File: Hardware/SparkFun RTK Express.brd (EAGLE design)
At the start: 68.2 x 110.1 mm, 198 parts, among them J13 Internal, J16 microSD, J17 Qwiic Right Angle, J19 FPC_12_0.5MM_BACKFLIP, J3 USB Female Type C Connector, J4 External, J5 USB Female Type C Connector, Q1 SIL2308-TP, Q10 20V/0.2A/8MHz/1.2Ω/1Vth, Q2 MBT3904DW1T1, Q3 20V/0.2A/8MHz/1.2Ω/1Vth, Q4 20V/0.2A/8MHz/1.2Ω/1Vth, Q7 20V/0.2A/8MHz/1.2Ω/1Vth, Q9 20V/0.2A/8MHz/1.2Ω/1Vth, U1 74HC4052D, U10 MCP73833, U13 9DoF IMU, U14 1.8V/100mA, U2 AP2112K-3.3, U3 U-BLOX_ZED-F9P, U4 ADP160, U5 ESP-WROOM-32NARROW, U6 CH340C, U7 MAX17048

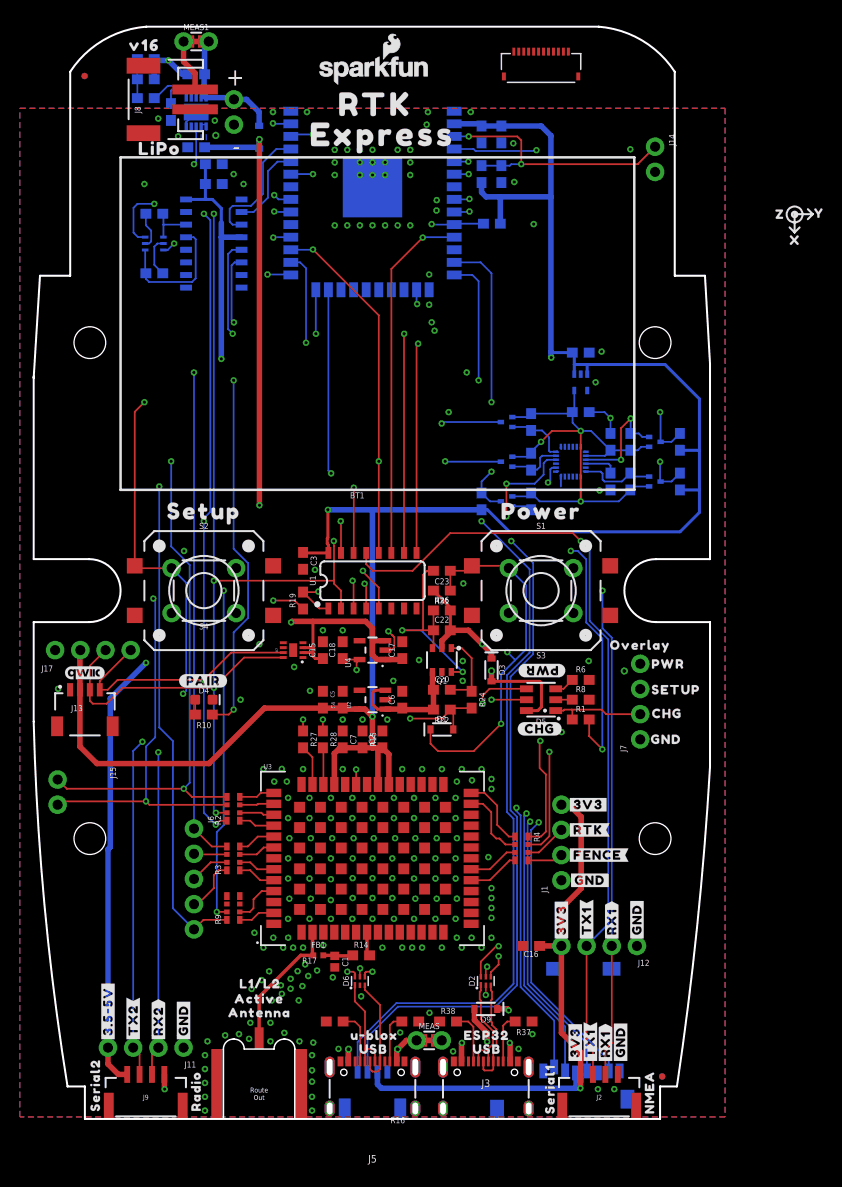
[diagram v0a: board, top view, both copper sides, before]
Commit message: Ready v11. Redo GND layers for panelizer.
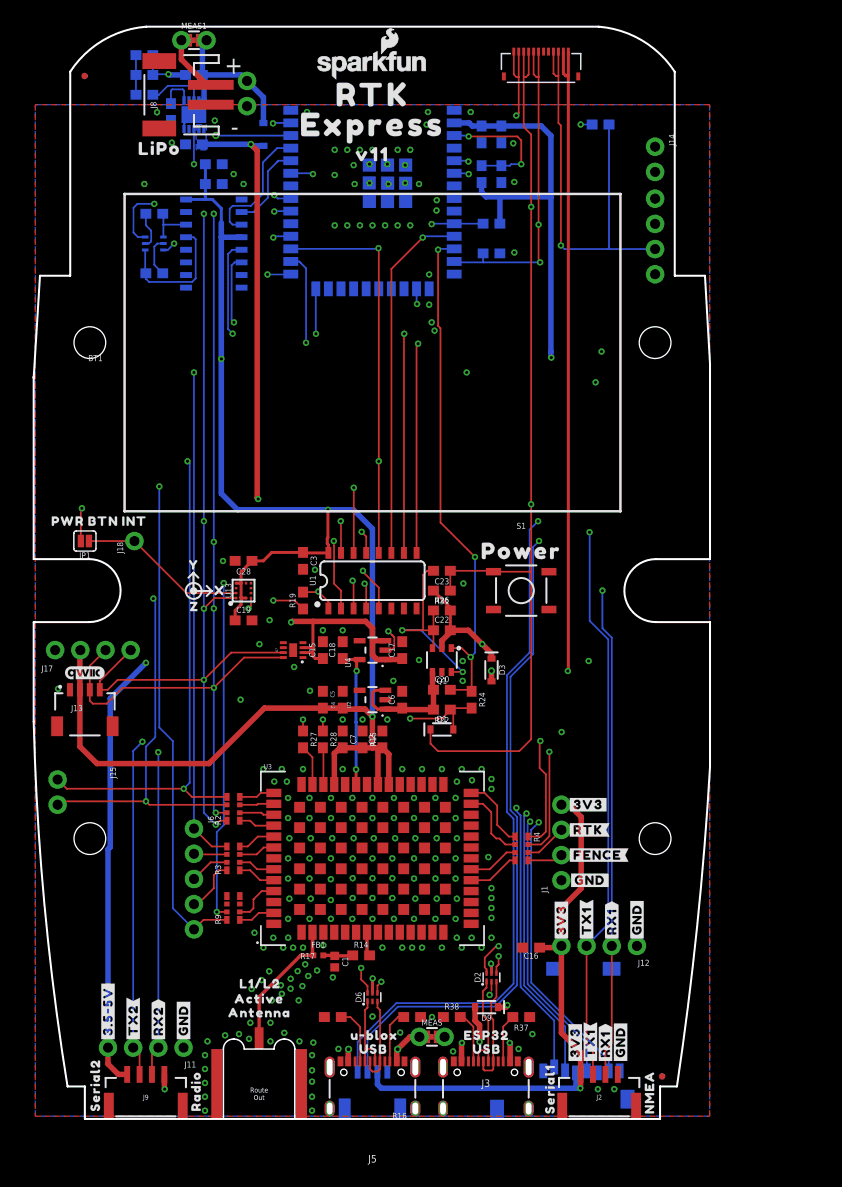
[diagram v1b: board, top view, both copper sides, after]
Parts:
- removed C51, C52: 0.1uF, SparkFun-Capacitors:0603
- removed C53, C54: 1.0uF, SparkFun-Capacitors:0603
- removed D4: BLUE, SparkFun-LED:LED-0603
- removed D5: RGB, SparkFun-LED:PLCC-6-LED
- removed Q10, Q3, Q4, Q7, Q9: 20V/0.2A/8MHz/1.2Ω/1Vth, SparkFun-DiscreteSemi:SOT-416FL
- removed R10: 330, SparkFun-Resistors:0603
- removed R40, R41, R44, R45, R46, R47, R48: 2.2k, SparkFun-Resistors:0603
- removed R49: (no value), SparkFun-Resistors:0603
- removed R6, R8: 1k, SparkFun-Resistors:0603
- removed S2: Setup, SparkFun-Switches:TACTILE_SWITCH_PTH_6.0MM
- removed S3: Power, SparkFun-Switches:TACTILE_SWITCH_SMD_12MM
- removed S4: Setup, SparkFun-Switches:TACTILE_SWITCH_SMD_12MM
- removed U$12, U$22: (no value), output:X1
- removed U$13, U$76: (no value), SparkFun GPS RTK Surveyor:LIGHT_PIPE_3MM
- removed U$15, U$21: (no value), output:Y2
- removed U$20: (no value), output:#PAIR#0
- removed U$25: (no value), output:#PWR#2
- removed U$44: (no value), output:OVERLAY0
- removed U$52, U$54: (no value), output:Z0
- removed U$95: (no value), output:AG0
- removed U$96: (no value), output:M0
- removed U14: 1.8V/100mA, SparkFun-IC-Power:SC70
- added C19: 10uF, SparkFun-Capacitors:0603
- added C21, C28: 0.1uF, SparkFun-Capacitors:0603
- added J18: (no value), SparkFun-Connectors:1X01_NO_SILK
- added JP1: (no value), SparkFun-Jumpers:SMT-JUMPER_2_NO_SILK
- BT1: value LIPO-OUTLINE1100 -> LIPO-OUTLINE1000
- R1: value 4.7k -> 470
- S1: device SparkFun-Switches:TACTILE_SWITCH_PTH_6.0MM -> SparkFun-Switches:TACTILE_SWITCH_SMD_5.2MM
- U$4: device output:V160 -> output:INT0
- U$8: device output:#CHG#0 -> output:V110
- U$9: device output:SETUP0 -> output:PWR_BTN1
- U13: value 9DoF IMU -> LIS2DH12; device SparkFun-Sensors:QFN24-3X3-ICM-20948 -> SparkFun-Sensors:LGA-12-LISDH12
- U5: value ESP-WROOM-32NARROW -> ESP-WROOM-3232D-NARROW; device SparkFun-RF:ESP-WROOM-32-NARROW -> SparkFun-RF:ESP-WROOM-32D-NARROW
- moved U$55 72.3 mm to (17.0, 55.6)
- moved U$56 71.1 mm to (16.9, 51.4)
- moved U$24 67.8 mm to (19.6, 53.0), turned to 0 degrees
- moved U$8 60.3 mm to (35.0, 97.0)
- moved R1 60.0 mm to (58.0, 100.0), flipped to the bottom
- moved U$4 48.0 mm to (11.0, 60.0)
- moved U$42 47.2 mm to (59.9, 89.9), flipped to the bottom
- moved U$41 47.1 mm to (60.7, 92.5), flipped to the bottom
- moved U$33 47.1 mm to (60.8, 87.5), flipped to the bottom
- moved U$34 47.0 mm to (60.9, 84.9), flipped to the bottom
- moved J7 46.9 mm to (63.5, 84.9), flipped to the bottom
- moved U$53 44.0 mm to (35.0, 50.0)
- moved U13 35.5 mm to (22.0, 53.0), flipped to the top, turned to 90 degrees
- moved BT1 29.8 mm to (35.0, 77.0)
- moved U$9 12.0 mm to (6.00, 60.0)
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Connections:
- net RTC_BACKUP renamed V_BKCP
- removed net ESP_12/LED_BLUETOOTH: R10.1, U5.14
- removed net ESP_15/ICM_!CS!: Q9.3, R47.1, U5.23
- removed net ESP_32/PWR_LVL_RED: D5.AR, U5.8
- removed net ESP_33/PWR_LVL_GRN: D5.AG, U5.9
- removed net ESP_I36/ICM_INT: Q7.3, R45.1, U5.4
- removed net ICM-20948-LV_!CS!: Q9.2, R46.1, U13.22
- removed net ICM-20948-LV_#_1.8V: C52.1, C53.1, Q10.1, Q3.1, Q4.1, Q7.1, Q9.1, R40.2, R41.2, R44.2, R46.2, R48.2, U13.13, U13.8, U14.5
- removed net ICM-20948-LV_INT: Q7.2, R44.1, U13.12
- removed net ICM-20948-LV_SCK: Q3.2, R40.1, U13.23
- removed net ICM-20948-LV_SDI: Q4.2, R41.1, U13.24
- removed net ICM-20948-LV_SDO: Q10.2, R48.1, U13.9
- removed net N$10: D5.CG, R6.1
- removed net N$14: D5.CR, R8.1
- removed net N$3: D4.A, R10.2
- removed net N$30: C51.1, U13.10
- new net ESP_12: U5.14
- new net ESP_15: U5.23
- new net ESP_32: U5.8
- new net ESP_33: U5.9
- new net ESP_4/ACCEL_INT: J18.1, JP1.1, U13.12
- new net ESP_I36: U5.4
- net 3.3V: now also C19.1, C28.1, U13.10, U13.2, U13.3, U13.9; no longer C54.1, R45.2, R47.2, R49.2, U14.1, U14.3
- net CHG_LED: no longer J19.10, J19.9
- net CHG_LED_RES: now also J19.10, J19.9; no longer D5.CB
- net ESP_14/SETUP_BUTTON: now also C21.1; no longer S2.1, S4.1
- net ESP_18/SCK: no longer Q3.3
- net ESP_19/CIPO: no longer Q10.3, R49.1
- net ESP_21/SDA: now also U13.4
- net ESP_22/SCL: now also U13.1
- net ESP_23/COPI: no longer Q4.3
- net GND: now also C19.2, C21.2, C28.2, U13.5, U13.6, U13.7, U13.8, U5.GND1, U5.GNDT1, U5.GNDT2, U5.GNDT3, U5.GNDT4, U5.GNDT5, U5.GNDT6, U5.GNDT7, U5.GNDT8; no longer C51.2, C52.2, C53.2, C54.2, D4.C, R6.2, R8.2, S2.3, S3.3, S4.3, U13.18, U13.20, U14.2, U5.GND
- net POWER_BTN: now also JP1.2; no longer S3.1
- net V_USB: no longer D5.AB
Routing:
- net POWER_BTN: track 50.7 -> 157.1 mm, vias 2 -> 3
- net ESP_14/SETUP_BUTTON: track 133.0 -> 45.6 mm, vias 3 -> 2
- net ESP_12/LED_BLUETOOTH: track 74.2 -> 0.00 mm, vias 3 -> 0
- net CHG_LED: track 107.6 -> 46.5 mm, vias 4 -> 2
- net ESP_33/PWR_LVL_GRN: track 60.9 -> 0.00 mm, vias 2 -> 0
- net ESP_32/PWR_LVL_RED: track 60.8 -> 0.00 mm, vias 2 -> 0
- net ESP_I36/ICM_INT: track 55.0 -> 0.00 mm, vias 3 -> 0
- net ICM-20948-LV_#_1.8V: track 53.9 -> 0.00 mm, vias 3 -> 0
- net V_USB: track 95.3 -> 140.7 mm
- net ESP_27/FAST_OFF: track 8.03 -> 52.5 mm, vias 0 -> 3
- net ESP_15/ICM_!CS!: track 39.7 -> 0.00 mm, vias 2 -> 0
- net CHG_LED_RES: track 9.78 -> 44.7 mm, vias 0 -> 1
- net 3.3V: track 349.6 -> 317.2 mm
- net ESP_19/CIPO: track 143.0 -> 115.7 mm, vias 5 -> 3
- net ESP_4/ACCEL_INT: track 0.00 -> 17.0 mm
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
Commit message: Update FP and PROD ID on ESP32 module
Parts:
- U4: value ADP160 -> STLQ015-3.3V
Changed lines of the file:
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@@
 <setting verticaltext="up"/>
 </settings>
-<grid distance="1" unitdist="mm" unit="mm" style="lines" multiple="1" display="yes" altdistance="0.1" altunitdist="mm" altunit="mm"/>
+<grid distance="0.05" unitdist="inch" unit="inch" style="lines" multiple="1" display="yes" altdistance="0.005" altunitdist="inch" altunit="inch"/>
 <layers>
 <layer number="1" name="Top/Horz" color="4" fill="1" visible="yes" active="yes"/>
-<layer number="2" name="GND/Horz" color="1" fill="3" visible="yes" active="yes"/>
-<layer number="15" name="Vert" color="4" fill="6" visible="yes" active="yes"/>
+<layer number="2" name="GND/Horz" color="1" fill="3" visible="no" active="yes"/>
+<layer number="15" name="Vert" color="4" fill="6" visible="no" active="yes"/>
 <layer number="16" name="Bottom/Vert" color="1" fill="1" visible="yes" active="yes"/>
 <layer number="17" name="Pads" color="2" fill="1" visible="yes" active="yes"/>
@@
 <attribute name="VALUE" value="470" x="58" y="99.238" size="0.6096" layer="28" font="vector" ratio="20" rot="MR0" align="top-center"/>
 </element>
-<element name="U4" library="SparkFun-IC-Power" package="SOT23-5" value="ADP160" x="35" y="47" smashed="yes" rot="R90">
+<element name="U4" library="SparkFun-IC-Power" package="SOT23-5" value="STLQ015-3.3V" x="35" y="47" smashed="yes" rot="R90">
 <attribute name="NAME" x="32.841" y="45.222" size="0.6096" layer="25" ratio="20" rot="R90"/>
-<attribute name="PROD_ID" value="VREG-11306" x="35" y="47" size="1.778" layer="27" font="vector" ratio="15" rot="R90" display="off"/>
-<attribute name="VALUE" value="ADP160" x="37.794" y="45.222" size="0.6096" layer="27" ratio="20" rot="R90"/>
+<attribute name="PROD_ID" value="IC-15779" x="35" y="47" size="1.778" layer="27" font="vector" ratio="15" rot="R90" display="off"/>
 </element>
 <element name="C17" library="SparkFun-Capacitors" package="0603" value="1.0uF" x="38" y="47" smashed="yes" rot="R90">
@@
 <element name="U5" library="SparkFun-RF" package="ESP-WROOM-32D-NARROW" value="ESP-WROOM-3232D-NARROW" x="35" y="95" smashed="yes" rot="MR90">
 <attribute name="NAME" x="35" y="85.97" size="0.8128" layer="26" rot="MR180" align="center"/>
-<attribute name="PROD_ID" value="IC-13849" x="35" y="95" size="1.778" layer="28" font="vector" ratio="15" rot="MR90" display="off"/>
+<attribute name="PROD_ID" value="IC-15676" x="35" y="95" size="1.778" layer="28" font="vector" ratio="15" rot="MR90" display="off"/>
 <attribute name="VALUE" x="35" y="87.24" size="0.8128" layer="28" rot="MR180" align="center"/>
 </element>

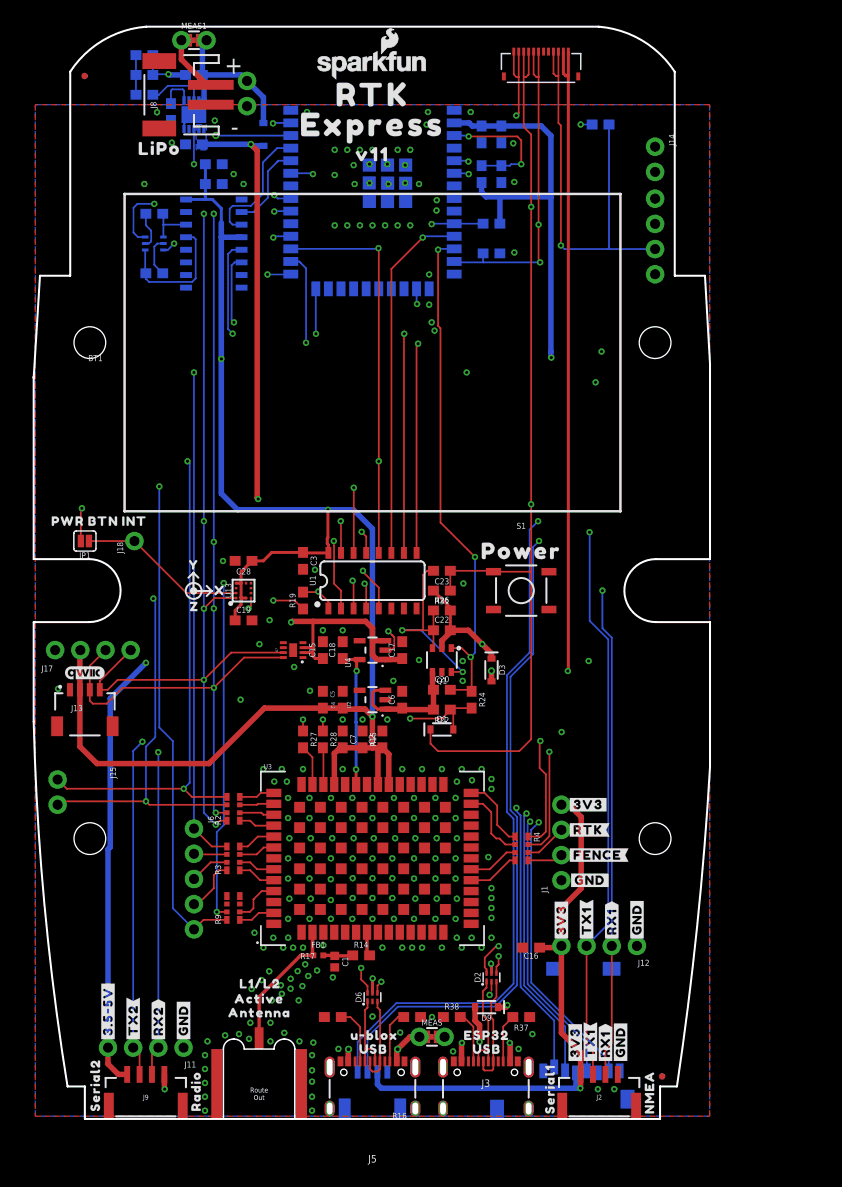
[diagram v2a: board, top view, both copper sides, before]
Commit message: Move radio to power control. Add ESD to GNSS RF. Move overlay connector.
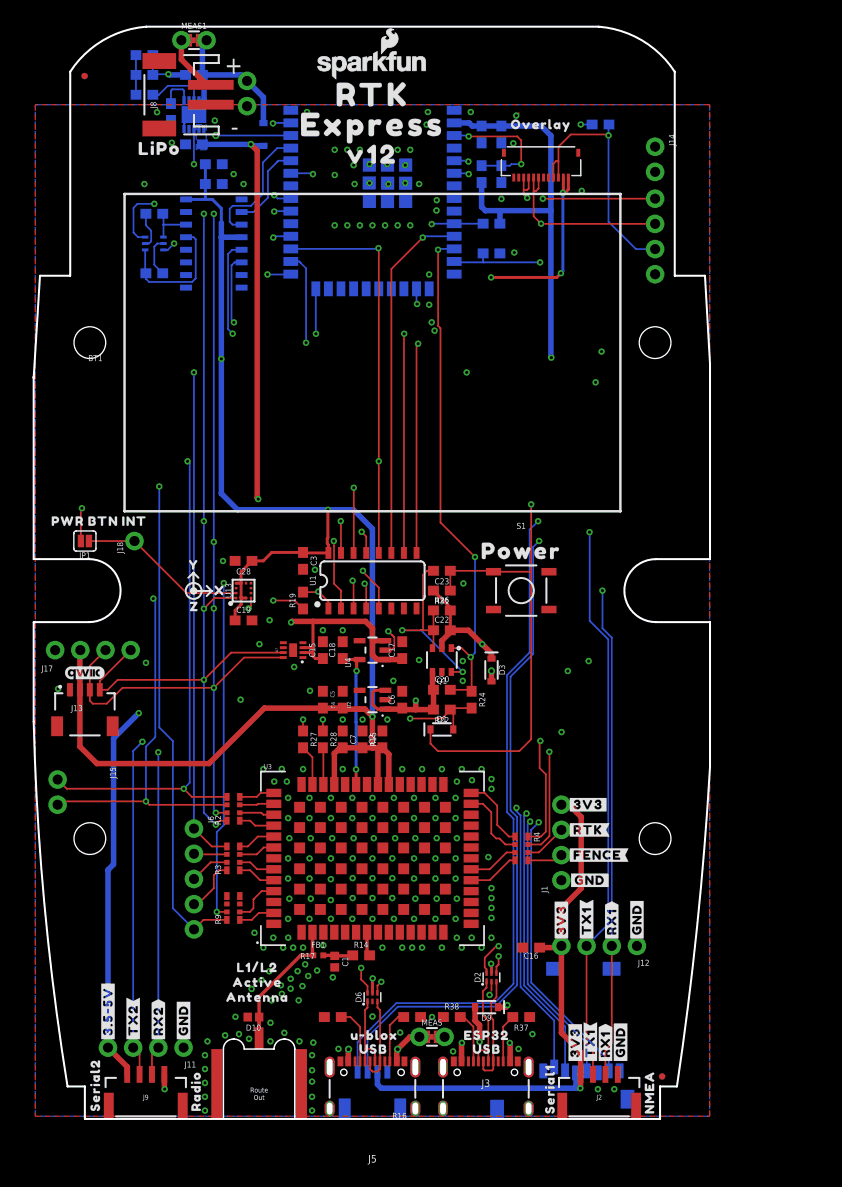
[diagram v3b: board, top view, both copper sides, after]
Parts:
- removed J19: FPC_12_0.5MM_BACKFLIP, RTK Facet:FPC_12_DOUBLESIDED_BACKFLIP
- removed U$18: (no value), output:ACTIVE0
- removed U$19: (no value), output:L1#L21
- added D10: PESD0402, New_Parts:0402
- added J20: FPC_12_0.5MM_BACKFLIP, RTK Facet:FPC_12_DOUBLESIDED_BACKFLIP
- added U$12: (no value), output:V120
- added U$13: (no value), output:ACTIVE1
- added U$15: (no value), output:ANTENNA2
- U$6: device output:ANTENNA0 -> output:L1#L20
- U$8: device output:V110 -> output:OVERLAY0
- moved U$8 17.3 mm to (52.0, 100.0)
- moved U$6 5.84 mm to (23.4, 15.0)
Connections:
- net CHG_LED_RES: now also J20.3, J20.4; no longer J19.10, J19.9
- net ESP_14/SETUP_BUTTON: now also J20.7, J20.8; no longer J19.5, J19.6
- net GND: now also D10.2, J20.11, J20.12; no longer J19.1, J19.2
- net GPS_ANT1: now also D10.1
- net POWER_BTN: now also J20.10, J20.9; no longer J19.3, J19.4
- net VOUT: now also J11.4, J9.1
- net V_RAW: no longer J11.4, J9.1
- net V_USB: now also J20.1, J20.2; no longer J19.11, J19.12
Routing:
- net VOUT: track 12.9 -> 80.8 mm, vias 0 -> 2
- net V_RAW: track 148.6 -> 104.2 mm
- net CHG_LED_RES: track 44.7 -> 26.4 mm
- net POWER_BTN: track 157.1 -> 143.0 mm, vias 3 -> 4
- net ESP_14/SETUP_BUTTON: track 45.6 -> 31.7 mm
- net GND: track 27.2 -> 18.1 mm, vias 204 -> 205
- net V_USB: track 140.7 -> 134.0 mm, vias 6 -> 9
- net GPS_ANT1: track 13.7 -> 15.9 mm
- net ESP_13/POWER_CTRL: track 52.4 -> 53.3 mm

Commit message: Add PROD_ID for PESD diode.
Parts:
- D10: device New_Parts:0402 -> SparkFun-DiscreteSemi:0402

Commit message: Shuffle schematic elements to fit into frame.
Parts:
- removed FRAME1: FRAME-LETTERNO_PACKAGE, SparkFun-Aesthetics:DUMMY
- added FRAME3: FRAME-LEDGERNO_FOOTPRINT, SparkFun-Aesthetics:DUMMY
- J20: value FPC_12_0.5MM_BACKFLIP -> (none)
